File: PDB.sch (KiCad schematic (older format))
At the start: 6 parts, among them J1 Conn_01x02, J2 Conn_01x02, J3 Conn_01x02, J4 Conn_01x02

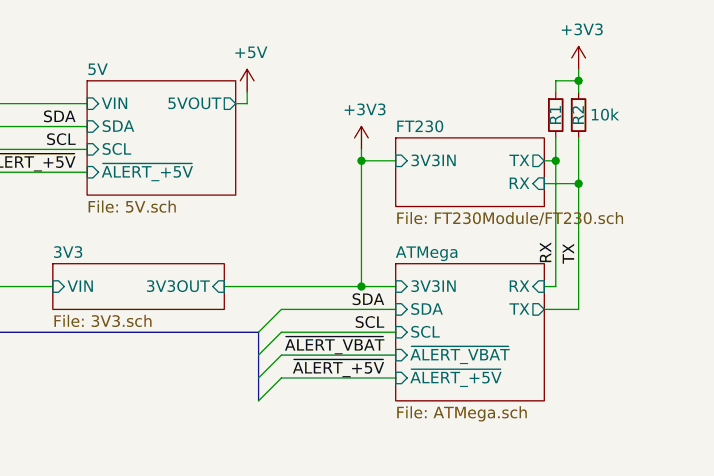
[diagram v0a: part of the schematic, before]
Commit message: remove isolation from FT230
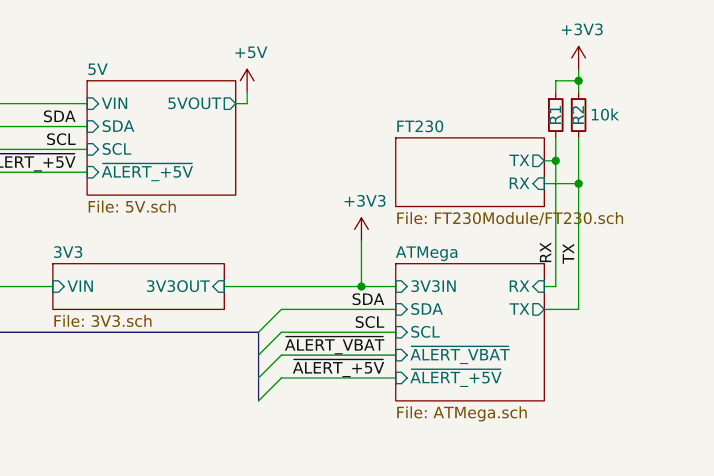
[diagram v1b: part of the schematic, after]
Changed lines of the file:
@@
 L power:+3V3 #PWR09
 U 1 1 5C347B0C
-P 7750 2400
-F 0 "#PWR09" H 7750 2250 50  0001 C CNN
-F 1 "+3V3" H 7765 2573 50  0000 C CNN
-F 2 "" H 7750 2400 50  0001 C CNN
-F 3 "" H 7750 2400 50  0001 C CNN
-	1    7750 2400
+P 7750 2800
+F 0 "#PWR09" H 7750 2650 50  0001 C CNN
+F 1 "+3V3" H 7765 2973 50  0000 C CNN
+F 2 "" H 7750 2800 50  0001 C CNN
+F 3 "" H 7750 2800 50  0001 C CNN
+	1    7750 2800
 	1    0    0    -1
 $EndComp
@@
 F2 "TX" O R 8550 2450 50
 F3 "RX" I R 8550 2550 50
-F4 "3V3IN" I L 7900 2450 50
 $EndSheet
 Connection ~ 5850 2200
-Wire Wire Line
-	7750 3000 7750 2450
-Wire Wire Line
-	7750 2450 7900 2450
-Connection ~ 7750 3000
-Wire Wire Line
-	7750 3000 7900 3000
-Wire Wire Line
-	7750 2450 7750 2400
-Connection ~ 7750 2450
-Wire Wire Line
-	7150 3000 7750 3000
 Wire Wire Line
 	8550 3000 8600 3000
@@
 	-1   0    0    -1
 $EndComp
+Wire Wire Line
+	7150 3000 7750 3000
+Wire Wire Line
+	7750 2800 7750 3000
 Wire Bus Line
 	4300 2400 4300 2700
@@
 Wire Bus Line
 	7300 3200 7300 3500
+Connection ~ 7750 3000
+Wire Wire Line
+	7750 3000 7900 3000
 $EndSCHEMATC

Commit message: layout
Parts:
- added H1, H2, H3, H4, H5, H6: MountingHole, MountingHole:MountingHole_3.2mm_M3, symbol Mechanical:MountingHole
- added J4, J5: Conn_01x02, XT30:XT30PB-F, symbol Connector_Generic:Conn_01x02
- added J6, J7: Conn_01x02, Connector_PinHeader_2.54mm:PinHeader_1x02_P2.54mm_Vertical, symbol Connector_Generic:Conn_01x02
- renumbered J4 to J8
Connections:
- net +5V: now also J4.2 (Pin_2), J5.2 (Pin_2)
- net GND: now also J4.1 (Pin_1), J5.1 (Pin_1), J6.1 (Pin_1), J7.1 (Pin_1)
- new net +BATT: J6.2 (Pin_2), J7.2 (Pin_2)
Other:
- note added: "Pin Header (VBAT):\nCam\nVTX"
- note added: "XT30 (5V):\nFC\nFCP\nNAV\nRECV\nLED"

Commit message: even more layout
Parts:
- added D11, D12, D13: LED, LED_SMD:LED_0603_1608Metric, symbol Device:LED
- added JP1, JP2: Jumper, Connector_PinHeader_2.54mm:PinHeader_1x02_P2.54mm_Vertical, symbol Device:Jumper
- added R28, R29: 470, Resistor_SMD:R_0603_1608Metric, symbol Device:R
- added R30: 270, Resistor_SMD:R_0603_1608Metric, symbol Device:R
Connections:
- net +3V3: now also R30.1
- net +5V: now also R29.1
- net +BATT: now also R28.1
- net GND: now also D11.1 (K), D12.1 (K), D13.1 (K), JP2.2
- new net: D11.2 (A), R28.2
- new net: D12.2 (A), R29.2
- new net: D13.2 (A), R30.2
- new net 5V/5VIN: JP1.2
- new net FT230/5VOUT: JP1.1
- new net GNDS: JP2.1
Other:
- note added: "Close jumpers to power\ndevice from USB port"
- note added: "REMOVE BEFORE FLIGHT"

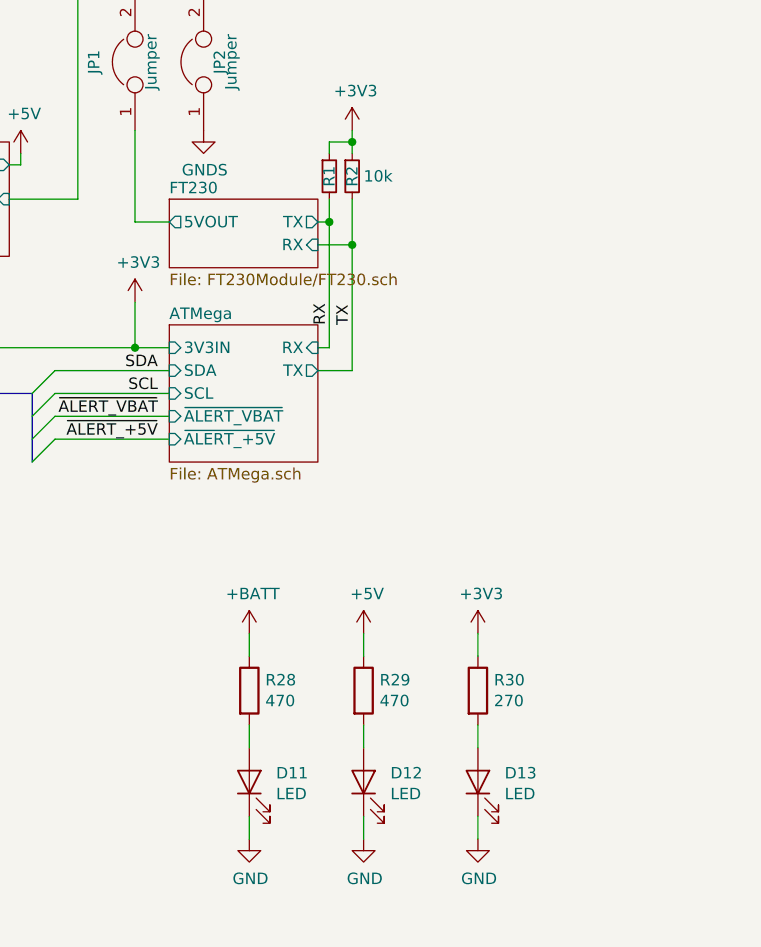
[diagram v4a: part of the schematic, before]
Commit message: layout fixes, reannotate
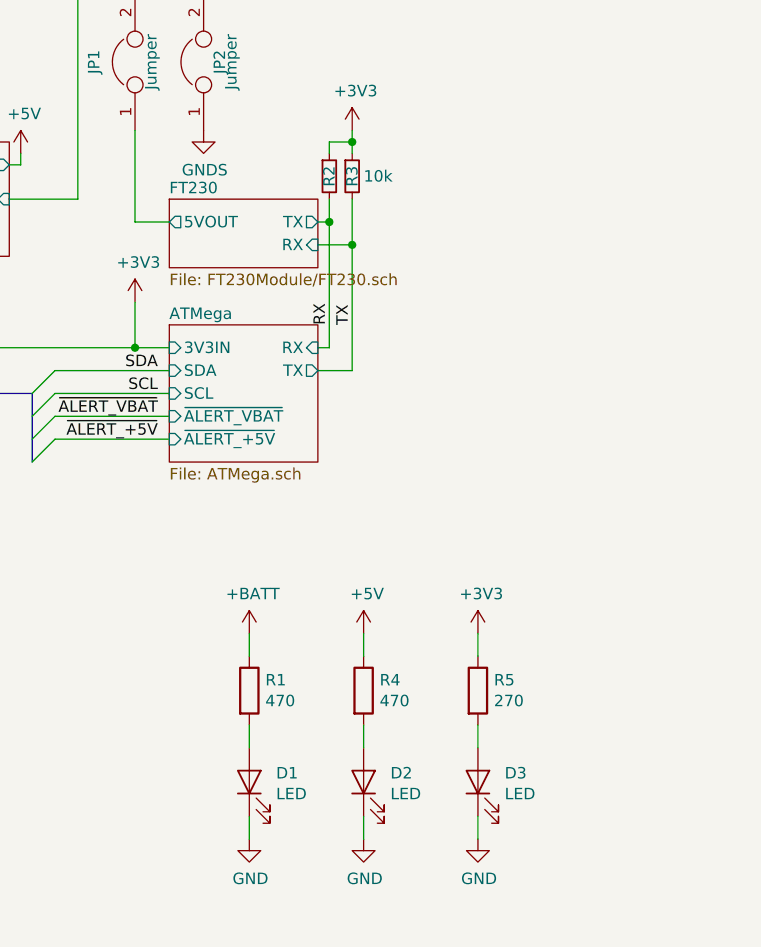
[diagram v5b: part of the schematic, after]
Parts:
- renumbered D11 to D1, D12 to D2, D13 to D3, R28 to R1, R1 to R2, R2 to R3, R29 to R4, R30 to R5
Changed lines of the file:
@@
 	3950 2200 4950 2200
 $Comp
-L power:+3V3 #PWR018
+L power:+3V3 #PWR019
 U 1 1 5C347B0C
 P 7750 2800
-F 0 "#PWR018" H 7750 2650 50  0001 C CNN
+F 0 "#PWR019" H 7750 2650 50  0001 C CNN
 F 1 "+3V3" H 7765 2973 50  0000 C CNN
 F 2 "" H 7750 2800 50  0001 C CNN
@@
 	7250 2200 7250 2150
 $Comp
-L power:+5V #PWR017
+L power:+5V #PWR018
 U 1 1 5C3483F6
 P 7250 2150
-F 0 "#PWR017" H 7250 2000 50  0001 C CNN
+F 0 "#PWR018" H 7250 2000 50  0001 C CNN
 F 1 "+5V" H 7265 2323 50  0000 C CNN
 F 2 "" H 7250 2150 50  0001 C CNN
@@
 	8700 3100 8550 3100
 $Comp
-L Device:R_Small R1
+L Device:R_Small R2
 U 1 1 5C32B264
 P 8600 2250
-F 0 "R1" V 8600 2250 50  0000 C CNN
+F 0 "R2" V 8600 2250 50  0000 C CNN
 F 1 "10k" H 8659 2205 50  0001 L CNN
 F 2 "Resistor_SMD:R_0603_1608Metric" H 8600 2250 50  0001 C CNN
@@
 $EndComp
 $Comp
-L Device:R_Small R2
+L Device:R_Small R3
 U 1 1 5C32B2AA
 P 8700 2250
-F 0 "R2" V 8700 2250 50  0000 C CNN
+F 0 "R3" V 8700 2250 50  0000 C CNN
 F 1 "10k" H 8750 2250 50  0000 L CNN
 F 2 "Resistor_SMD:R_0603_1608Metric" H 8700 2250 50  0001 C CNN
@@
 Connection ~ 8700 2100
 $Comp
-L power:+3V3 #PWR019
+L power:+3V3 #PWR024
 U 1 1 5C32C866
 P 8700 2050
-F 0 "#PWR019" H 8700 1900 50  0001 C CNN
+F 0 "#PWR024" H 8700 1900 50  0001 C CNN
 F 1 "+3V3" H 8715 2223 50  0000 C CNN
 F 2 "" H 8700 2050 50  0001 C CNN
@@
 	3250 5200 3250 5250
 $Comp
-L power:+BATT #PWR016
+L power:+BATT #PWR017
 U 1 1 5CABEEB4
 P 6050 2100
-F 0 "#PWR016" H 6050 1950 50  0001 C CNN
+F 0 "#PWR017" H 6050 1950 50  0001 C CNN
 F 1 "+BATT" H 6065 2273 50  0000 C CNN
 F 2 "" H 6050 2100 50  0001 C CNN
@@
 $EndComp
 $Comp
-L Device:R R28
+L Device:R R1
 U 1 1 5CA79731
 P 8250 4500
-F 0 "R28" H 8320 4546 50  0000 L CNN
+F 0 "R1" H 8320 4546 50  0000 L CNN
 F 1 "470" H 8320 4455 50  0000 L CNN
 F 2 "Resistor_SMD:R_0603_1608Metric" V 8180 4500 50  0001 C CNN
@@
 $EndComp
 $Comp
-L Device:LED D11
+L Device:LED D1
 U 1 1 5CA7A26C
 P 8250 4900
-F 0 "D11" V 8289 4783 50  0000 R CNN
+F 0 "D1" V 8289 4783 50  0000 R CNN
 F 1 "LED" V 8198 4783 50  0000 R CNN
 F 2 "LED_SMD:LED_0603_1608Metric" H 8250 4900 50  0001 C CNN
@@
 P 8250 5150
 AR Path="/5C2F335D/5CA7EC16" Ref="#PWR?"  Part="1"
-AR Path="/5CA7EC16" Ref="#PWR0102"  Part="1"
-F 0 "#PWR0102" H 8250 4900 50  0001 C CNN
+AR Path="/5CA7EC16" Ref="#PWR023"  Part="1"
+F 0 "#PWR023" H 8250 4900 50  0001 C CNN
 F 1 "GND" H 8255 4977 50  0000 C CNN
 F 2 "" H 8250 5150 50  0001 C CNN
@@
 $EndComp
 $Comp
-L power:+5V #PWR0103
+L power:+5V #PWR025
 U 1 1 5CA7F0E2
 P 8750 4250
-F 0 "#PWR0103" H 8750 4100 50  0001 C CNN
+F 0 "#PWR025" H 8750 4100 50  0001 C CNN
 F 1 "+5V" H 8765 4423 50  0000 C CNN
 F 2 "" H 8750 4250 50  0001 C CNN
@@
 $EndComp
 $Comp
-L Device:R R29
+L Device:R R4
 U 1 1 5CA8354A
 P 8750 4500
-F 0 "R29" H 8820 4546 50  0000 L CNN
+F 0 "R4" H 8820 4546 50  0000 L CNN
 F 1 "470" H 8820 4455 50  0000 L CNN
 F 2 "Resistor_SMD:R_0603_1608Metric" V 8680 4500 50  0001 C CNN
@@
 $EndComp
 $Comp
-L Device:LED D12
+L Device:LED D2
 U 1 1 5CA83554
 P 8750 4900
-F 0 "D12" V 8789 4783 50  0000 R CNN
+F 0 "D2" V 8789 4783 50  0000 R CNN
 F 1 "LED" V 8698 4783 50  0000 R CNN
 F 2 "LED_SMD:LED_0603_1608Metric" H 8750 4900 50  0001 C CNN
@@
 P 8750 5150
 AR Path="/5C2F335D/5CA83561" Ref="#PWR?"  Part="1"
-AR Path="/5CA83561" Ref="#PWR0104"  Part="1"
-F 0 "#PWR0104" H 8750 4900 50  0001 C CNN
+AR Path="/5CA83561" Ref="#PWR026"  Part="1"
+F 0 "#PWR026" H 8750 4900 50  0001 C CNN
 F 1 "GND" H 8755 4977 50  0000 C CNN
 F 2 "" H 8750 5150 50  0001 C CNN
@@
 $EndComp
 $Comp
-L Device:R R30
+L Device:R R5
 U 1 1 5CA86515
 P 9250 4500
-F 0 "R30" H 9320 4546 50  0000 L CNN
+F 0 "R5" H 9320 4546 50  0000 L CNN
 F 1 "270" H 9320 4455 50  0000 L CNN
 F 2 "Resistor_SMD:R_0603_1608Metric" V 9180 4500 50  0001 C CNN
@@
 $EndComp
 $Comp
-L Device:LED D13
+L Device:LED D3
 U 1 1 5CA8651F
 P 9250 4900
-F 0 "D13" V 9289 4783 50  0000 R CNN
+F 0 "D3" V 9289 4783 50  0000 R CNN
 F 1 "LED" V 9198 4783 50  0000 R CNN
 F 2 "LED_SMD:LED_0603_1608Metric" H 9250 4900 50  0001 C CNN
@@
 P 9250 5150
 AR Path="/5C2F335D/5CA8652C" Ref="#PWR?"  Part="1"
-AR Path="/5CA8652C" Ref="#PWR0105"  Part="1"
-F 0 "#PWR0105" H 9250 4900 50  0001 C CNN
+AR Path="/5CA8652C" Ref="#PWR028"  Part="1"
+F 0 "#PWR028" H 9250 4900 50  0001 C CNN
 F 1 "GND" H 9255 4977 50  0000 C CNN
 F 2 "" H 9250 5150 50  0001 C CNN
@@
 $EndComp
 $Comp
-L power:+3V3 #PWR0106
+L power:+3V3 #PWR027
 U 1 1 5CA89CFD
 P 9250 4250
-F 0 "#PWR0106" H 9250 4100 50  0001 C CNN
+F 0 "#PWR027" H 9250 4100 50  0001 C CNN
 F 1 "+3V3" H 9265 4423 50  0000 C CNN
 F 2 "" H 9250 4250 50  0001 C CNN
@@
 $EndComp
 $Comp
-L power:+BATT #PWR0107
+L power:+BATT #PWR022
 U 1 1 5CA8A3F2
 P 8250 4250
-F 0 "#PWR0107" H 8250 4100 50  0001 C CNN
+F 0 "#PWR022" H 8250 4100 50  0001 C CNN
 F 1 "+BATT" H 8265 4423 50  0000 C CNN
 F 2 "" H 8250 4250 50  0001 C CNN
@@
 $EndComp
 $Comp
-L power:GND #PWR0110
+L power:GND #PWR020
 U 1 1 5CA8DA50
 P 8050 1450
-F 0 "#PWR0110" H 8050 1200 50  0001 C CNN
+F 0 "#PWR020" H 8050 1200 50  0001 C CNN
 F 1 "GND" H 8055 1277 50  0000 C CNN
 F 2 "" H 8050 1450 50  0001 C CNN
@@
 $EndComp
 $Comp
-L power:GNDS #PWR0111
+L power:GNDS #PWR021
 U 1 1 5CA8E60E
 P 8050 2050
-F 0 "#PWR0111" H 8050 1800 50  0001 C CNN
+F 0 "#PWR021" H 8050 1800 50  0001 C CNN
 F 1 "GNDS" H 8055 1877 50  0000 C CNN
 F 2 "" H 8050 2050 50  0001 C CNN
@@
 Wire Wire Line
 	5850 2150 5850 2100
+$Comp
+L power:+5V #PWR016
+U 1 1 5CAACC08
+P 5850 2100
+F 0 "#PWR016" H 5850 1950 50  0001 C CNN
+F 1 "+5V" H 5865 2273 50  0000 C CNN
+F 2 "" H 5850 2100 50  0001 C CNN
+F 3 "" H 5850 2100 50  0001 C CNN
+	1    5850 2100
+	1    0    0    -1
+$EndComp
 Wire Bus Line
 	4300 2400 4300 2700
@@
 Wire Bus Line
 	7300 3200 7300 3500
-$Comp
-L power:+5V #PWR?
-U 1 1 5CAACC08
-P 5850 2100
-F 0 "#PWR?" H 5850 1950 50  0001 C CNN
-F 1 "+5V" H 5865 2273 50  0000 C CNN
-F 2 "" H 5850 2100 50  0001 C CNN
-F 3 "" H 5850 2100 50  0001 C CNN
-	1    5850 2100
-	1    0    0    -1
-$EndComp
 $EndSCHEMATC

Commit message: use official XT30 footprint
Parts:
- J1, J2, J3, J4, J5: footprint XT30:XT30PB-F -> Connector_AMASS:AMASS_XT30UPB-F_1x02_P5.0mm_Vertical
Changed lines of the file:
@@
 F 0 "J2" H 2418 4875 50  0000 C CNN
 F 1 "Conn_01x02" H 2418 4966 50  0000 C CNN
-F 2 "XT30:XT30PB-F" H 2500 5200 50  0001 C CNN
+F 2 "Connector_AMASS:AMASS_XT30UPB-F_1x02_P5.0mm_Vertical" H 2500 5200 50  0001 C CNN
 F 3 "~" H 2500 5200 50  0001 C CNN
 	1    2500 5200
@@
 F 0 "J1" H 2418 4225 50  0000 C CNN
 F 1 "Conn_01x02" H 2418 4316 50  0000 C CNN
-F 2 "XT30:XT30PB-F" H 2500 4550 50  0001 C CNN
+F 2 "Connector_AMASS:AMASS_XT30UPB-F_1x02_P5.0mm_Vertical" H 2500 4550 50  0001 C CNN
 F 3 "~" H 2500 4550 50  0001 C CNN
 	1    2500 4550
@@
 F 0 "J3" H 2418 5525 50  0000 C CNN
 F 1 "Conn_01x02" H 2418 5616 50  0000 C CNN
-F 2 "XT30:XT30PB-F" H 2500 5850 50  0001 C CNN
+F 2 "Connector_AMASS:AMASS_XT30UPB-F_1x02_P5.0mm_Vertical" H 2500 5850 50  0001 C CNN
 F 3 "~" H 2500 5850 50  0001 C CNN
 	1    2500 5850
@@
 F 0 "J4" H 2418 6175 50  0000 C CNN
 F 1 "Conn_01x02" H 2418 6266 50  0000 C CNN
-F 2 "XT30:XT30PB-F" H 2500 6500 50  0001 C CNN
+F 2 "Connector_AMASS:AMASS_XT30UPB-F_1x02_P5.0mm_Vertical" H 2500 6500 50  0001 C CNN
 F 3 "~" H 2500 6500 50  0001 C CNN
 	1    2500 6500
@@
 F 0 "J5" H 2418 6825 50  0000 C CNN
 F 1 "Conn_01x02" H 2418 6916 50  0000 C CNN
-F 2 "XT30:XT30PB-F" H 2500 7150 50  0001 C CNN
+F 2 "Connector_AMASS:AMASS_XT30UPB-F_1x02_P5.0mm_Vertical" H 2500 7150 50  0001 C CNN
 F 3 "~" H 2500 7150 50  0001 C CNN
 	1    2500 7150

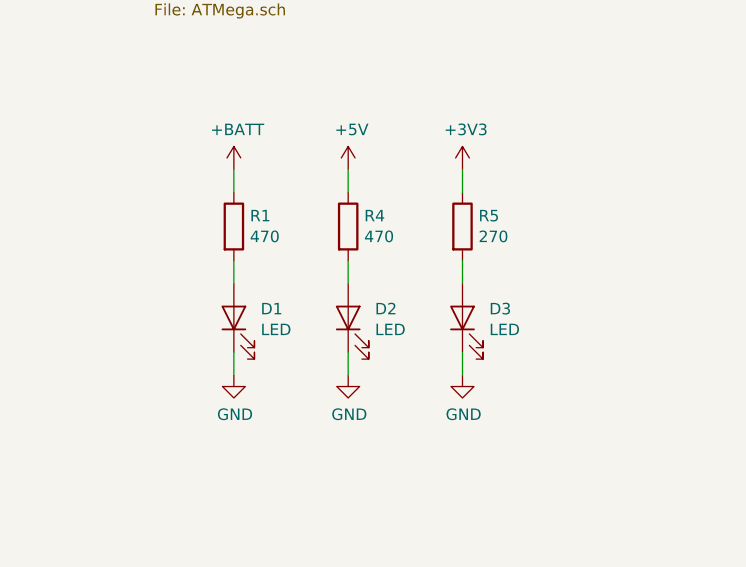
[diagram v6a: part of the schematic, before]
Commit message: fix LEDs
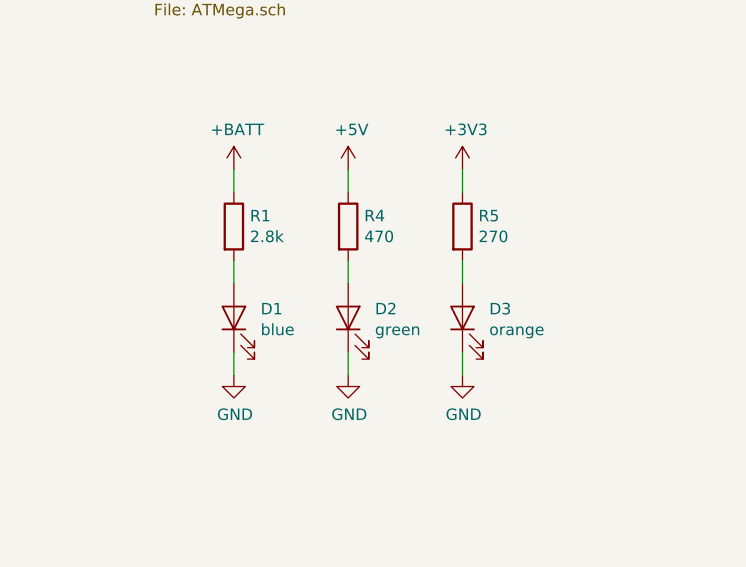
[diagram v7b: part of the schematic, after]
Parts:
- D1: value LED -> blue
- D2: value LED -> green
- D3: value LED -> orange
- R1: value 470 -> 2.8k
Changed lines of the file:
@@
 P 8250 4500
 F 0 "R1" H 8320 4546 50  0000 L CNN
-F 1 "470" H 8320 4455 50  0000 L CNN
+F 1 "2.8k" H 8320 4455 50  0000 L CNN
 F 2 "Resistor_SMD:R_0603_1608Metric" V 8180 4500 50  0001 C CNN
 F 3 "~" H 8250 4500 50  0001 C CNN
@@
 P 8250 4900
 F 0 "D1" V 8289 4783 50  0000 R CNN
-F 1 "LED" V 8198 4783 50  0000 R CNN
+F 1 "blue" V 8198 4783 50  0000 R CNN
 F 2 "LED_SMD:LED_0603_1608Metric" H 8250 4900 50  0001 C CNN
 F 3 "~" H 8250 4900 50  0001 C CNN
@@
 P 8750 4900
 F 0 "D2" V 8789 4783 50  0000 R CNN
-F 1 "LED" V 8698 4783 50  0000 R CNN
+F 1 "green" V 8698 4783 50  0000 R CNN
 F 2 "LED_SMD:LED_0603_1608Metric" H 8750 4900 50  0001 C CNN
 F 3 "~" H 8750 4900 50  0001 C CNN
@@
 P 9250 4900
 F 0 "D3" V 9289 4783 50  0000 R CNN
-F 1 "LED" V 9198 4783 50  0000 R CNN
+F 1 "orange" V 9198 4783 50  0000 R CNN
 F 2 "LED_SMD:LED_0603_1608Metric" H 9250 4900 50  0001 C CNN
 F 3 "~" H 9250 4900 50  0001 C CNN
